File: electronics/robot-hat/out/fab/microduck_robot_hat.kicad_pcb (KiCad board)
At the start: 2 copper layers, 65 x 30 mm, 28 parts, among them J1 40-pin GPIO, J2 VBAT in (B2B-XH-A), J3 DXL bus (B3B-EH-A), J5 Stemma J5 (SM04B-SRSS-TB), J6 speaker (B2B-PH-K-S), J7 mic (B3B-PH-K-S), U1 TLV320AIC3104, U2 Pololu D30V30F5, U3 BMI088 (dormant), U4 74LVC1G125

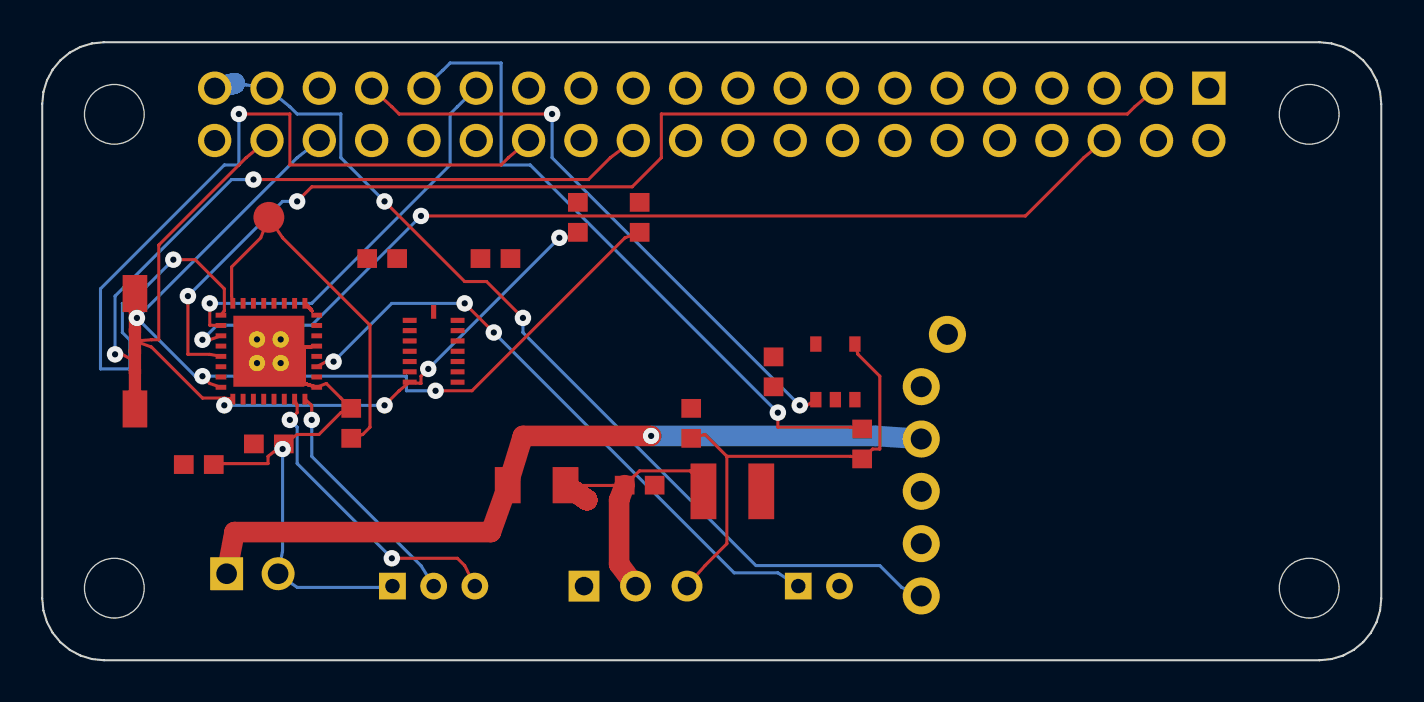
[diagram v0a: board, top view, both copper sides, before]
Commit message: rebuild round 2: ankle, thigh, foot, neck, hip links verified; trunk-base connector name swap fixed (verify agent's finding); electronics datasheet folders; wiring part records
Co-Authored-By: Claude Fable 5 <noreply@anthropic.com>
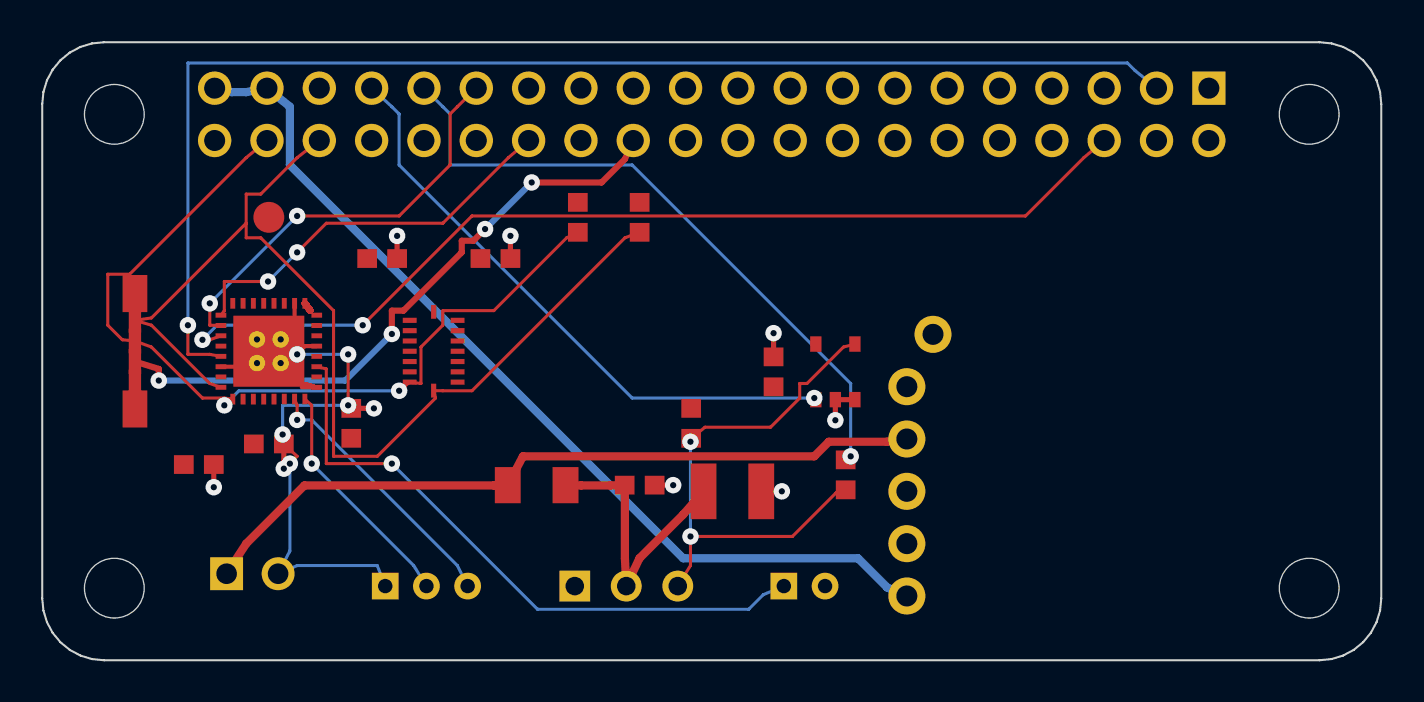
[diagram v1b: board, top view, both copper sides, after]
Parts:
- moved R4 1.70 mm to (39.0, -9.00)
- moved J6 0.70 mm to (37.0, -3.60)
- moved U2 0.70 mm to (49.6, -12.0)
- moved J3 0.45 mm to (28.4, -3.60)
- moved J7 0.35 mm to (18.6, -3.60)
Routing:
- net GND: track 154.8 -> 193.6 mm, vias 1 -> 14
- net i2s3/MCLK: track 45.1 -> 19.3 mm
- net HAT_1V8: track 18.1 -> 0.00 mm
- net SERVO_V: track 28.0 -> 13.8 mm
- net V5_HAT: track 58.0 -> 45.4 mm, vias 2 -> 0
- net HAT_3V3: track 69.9 -> 79.2 mm
- net i2c3/SCL: track 43.2 -> 51.8 mm, vias 3 -> 0
- net i2s3/DOUT: track 56.8 -> 63.2 mm, vias 2 -> 1
- net dxl/DATA: track 22.5 -> 26.0 mm, vias 0 -> 2
- net i2c3/SDA: track 40.2 -> 42.8 mm, vias 4 -> 2
- net VBAT: track 38.8 -> 36.1 mm, vias 1 -> 0
- net MICBIAS: track 14.7 -> 12.9 mm, vias 2 -> 1
- net J5_3V3: track 32.1 -> 30.8 mm, vias 2 -> 4
- net SPK_P: track 30.2 -> 30.6 mm, vias 3 -> 1
- net uart2/TX: track 29.2 -> 29.3 mm, vias 2 -> 1
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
